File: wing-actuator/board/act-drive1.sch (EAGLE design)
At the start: 104 parts, among them J1 POWER_JACKPTH_LOCK, Q1 BSS123, Q2 BSS123, U5 Q50-5C, U7 LP2985-33, U8 TPS62160, X1 SMA-142-0701-801/806, X2 SMA-142-0701-801/806, X3 SMA-142-0701-801/806, X4 SMA-142-0701-801/806, X5 2516-

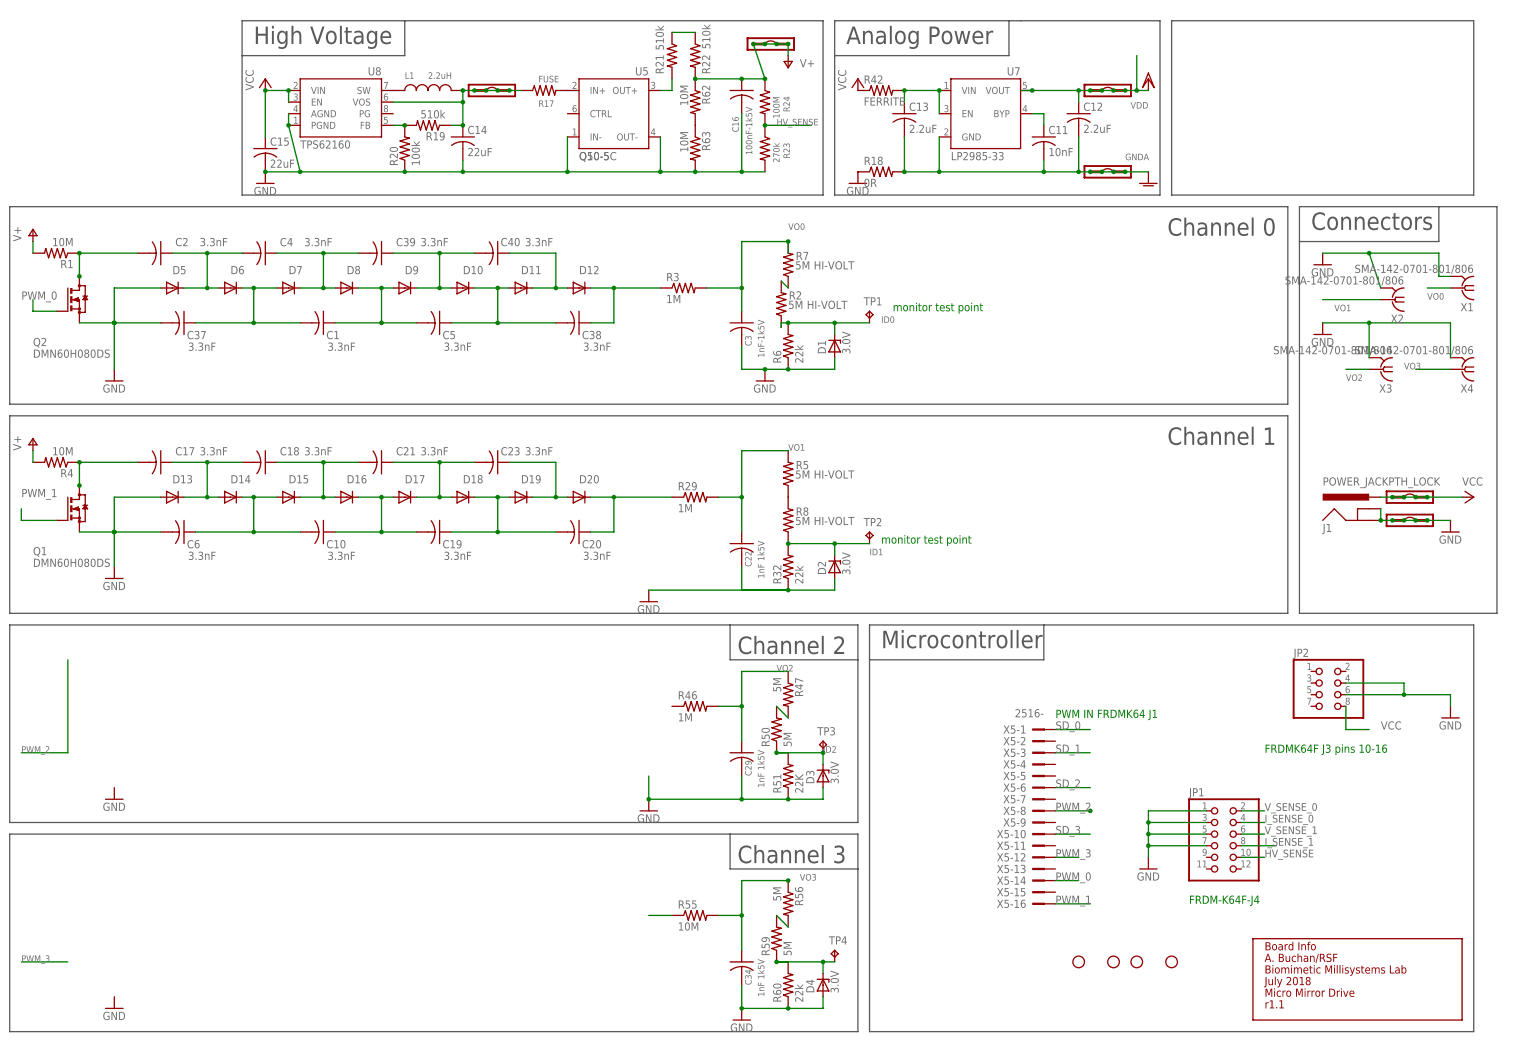
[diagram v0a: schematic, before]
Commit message: updated library to include 1:10 xfmr
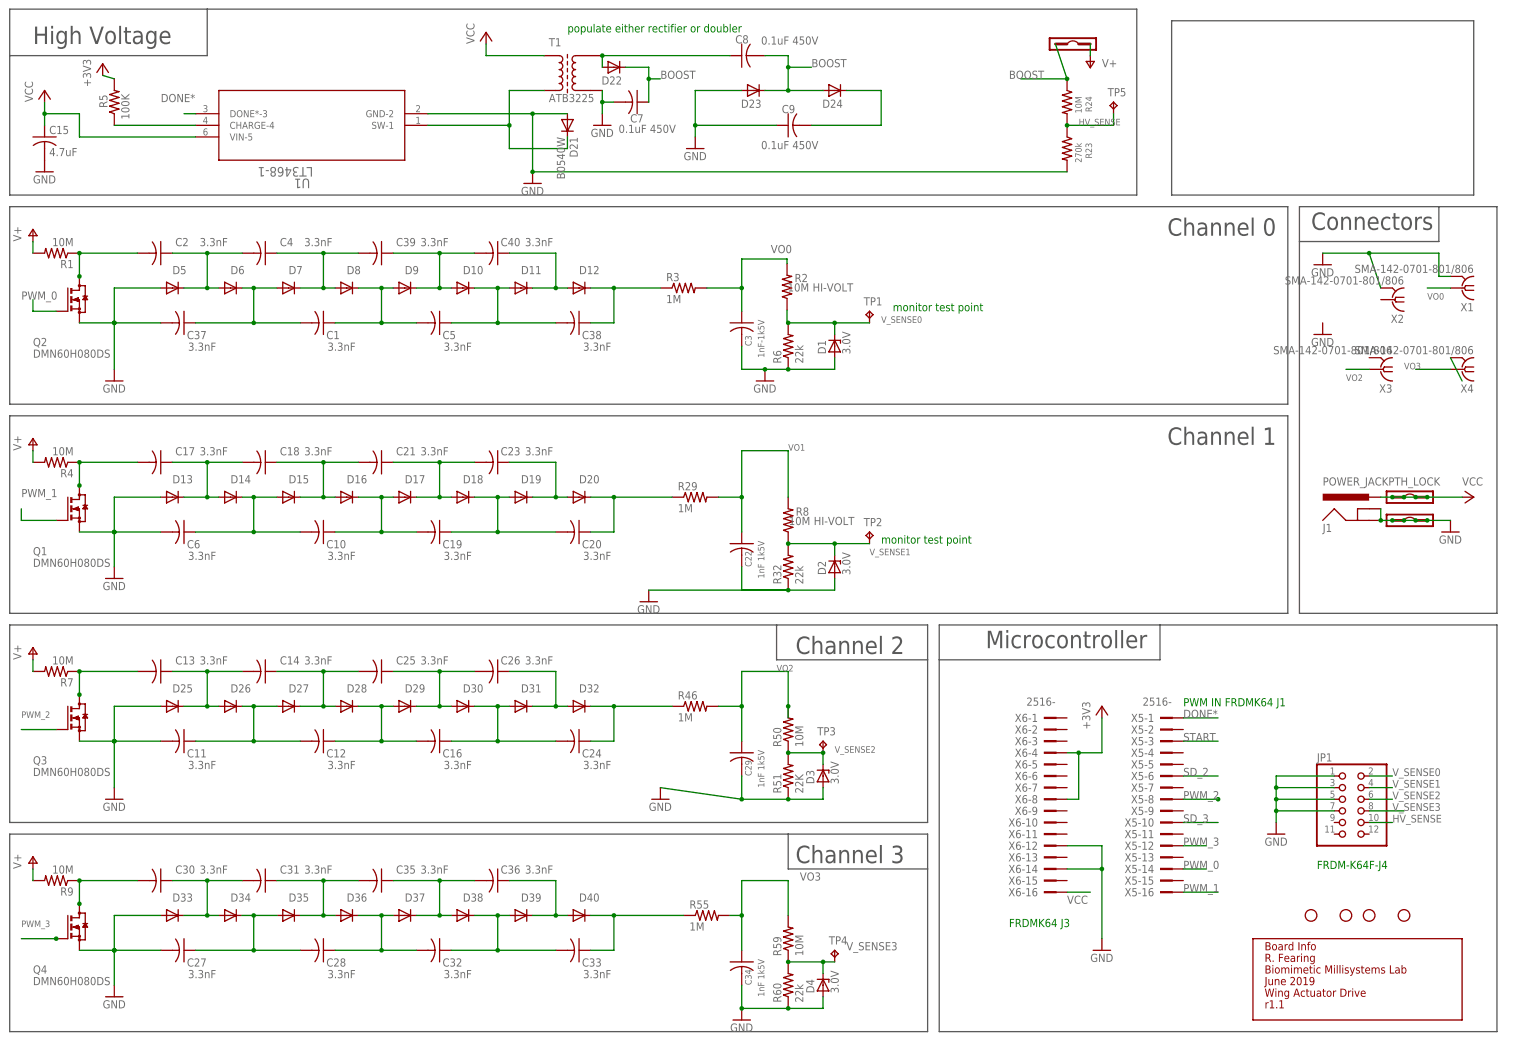
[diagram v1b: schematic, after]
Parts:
- removed GNDA, HV_IN, VDDA: (no value), modular_robotics:M04LOCK
- removed JP2: (no value), pinhead:PINHD-2X4
- removed L1: 2.2uH, modular_robotics:INDUCTOR
- removed R17: FUSE, rcl:R-US_R1206
- removed R18: 0R, rcl:R-US_R1206
- removed R19, R21, R22: 510k, rcl:R-US_R1206
- removed R20: 100k, rcl:R-US_R1206
- removed R42: FERRITE, rcl:R-US_R1206
- removed R47, R56: 5M, rcl:R-US_R1206
- removed R62, R63: 10M, rcl:R-US_R1206
- removed U5: Q50-5C, modular_robotics:Q50-5C
- removed U7: LP2985-33, modular_robotics:LP2985-33
- removed U8: TPS62160, modular_robotics:TPS62160
- added C24, C25, C26, C27, C28, C30, C31, C32, C33, C35, C36: 3.3nF, rcl:C-USC0805K
- added C7, C8, C9: 0.1uF 450V, rcl:C-USC1206
- added D21: B0540W, diode:DIODE-SOD123
- added D22, D23, D24, D25, D26, D27, D28, D29, D30, D31, D32, D33, D34, D35, D36, D37, D38, D39, D40: (no value), diode:DIODE-SOD323-W
- added Q3, Q4: BSS123, transistor-small-signal:BSS123
- added R9: 10M, rcl:R-US_R1206
- added T1: ATB3225, lt3468-1:ATB3225
- added TP5: TPTP10SQ, testpad:TPTP10SQ
- added U1: LT3468-1, ActuatorDrive:LT3468-1
- added X6: 2516-, con-3m:2516-
- C11: value 10nF -> 3.3nF; device rcl:C-USC1206 -> rcl:C-USC0805K
- C12, C13: value 2.2uF -> 3.3nF; device rcl:C-USC1206 -> rcl:C-USC0805K
- C14: value 22uF -> 3.3nF; device rcl:C-USC1206 -> rcl:C-USC0805K
- C15: value 22uF -> 4.7uF
- C16: value 100nF-1k5V -> 3.3nF; device rcl:C-USC2225K -> rcl:C-USC0805K
- R2, R50, R59: value 5M -> 10M; device rcl:R-US_R1206 -> rcl:R-US_R2010
- R24: value 100M -> 10M
- R5: value 5M -> 100K; device rcl:R-US_R1206 -> resistor:R-US_R1206; HI-VOLT 800 -> (none)
- R55: value 10M -> 1M
- R7: value 5M -> 10M; HI-VOLT 800 -> (none)
- R8: value 5M -> 10M; device rcl:R-US_R1206 -> rcl:R-US_R2010; HI-VOLT 800 -> 2000
- U$18: AUTHOR A. Buchan/RSF -> R. Fearing; DATE July 2018 -> June 2019; DESIGN Micro Mirror Drive -> Wing Actuator Drive
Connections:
- net SD_1 renamed START
- removed net GNDA: C11.2, C12.2, C13.2, GNDA.1, GNDA.2, GNDA.3, GNDA.4, R18.2, U7.GND
- removed net ID0: D1.C, R2.1, R6.2, TP1.TP
- removed net ID1: D2.C, R32.2, R8.1, TP2.TP
- removed net ID2: D3.C, R50.1, R51.2, TP3.TP
- removed net ID3: D4.C, R59.1, R60.2, TP4.TP
- removed net I_SENSE_0: JP1.4
- removed net I_SENSE_1: JP1.8
- removed net N$60: R21.2, U5.OUT+
- removed net N$62: R62.2, R63.1
- removed net SD_0: X5-1.KL
- removed net VDDA: C12.1, U7.VOUT, VDDA.1, VDDA.2, VDDA.3, VDDA.4
- removed net V_SENSE_0: JP1.2
- removed net V_SENSE_1: JP1.6
- new net +3V3: R5.2, X6-4.KL, X6-8.KL
- new net BOOST: C7.1, C8.2, D22.C, D23.C, D24.A, HV_OUT.4, R24.1
- new net DONE*: R5.1, U1.CHARGE-4, U1.DONE*-3, X5-1.KL
- new net N$28: X4.2
- new net N$29: C25.1, C26.2, D29.C, D30.A
- new net N$30: C13.2, Q3.D, R7.1
- new net N$32: C30.1, C31.2, D33.C, D34.A
- new net N$33: C27.1, C28.2, D34.C, D35.A
- new net N$34: C36.1, D39.C, D40.A
- new net N$35: C28.1, C32.2, D36.C, D37.A
- new net N$36: C32.1, C33.2, D38.C, D39.A
- new net N$38: C35.1, C36.2, D37.C, D38.A
- new net N$39: C30.2, Q4.D, R9.1
- new net V_SENSE0: D1.C, JP1.2, R2.1, R6.2, TP1.TP
- new net V_SENSE1: D2.C, JP1.4, R32.2, R8.1, TP2.TP
- new net V_SENSE2: D3.C, JP1.6, R50.1, R51.2, TP3.TP
- new net V_SENSE3: D4.C, JP1.8, R59.1, R60.2, TP4.TP
- net GND: now also C11.2, C27.2, C7.2, C9.1, D21.A, D23.A, D25.A, D33.A, Q3.S, Q4.S, T1.S3, X6-12.KL, X6-14.KL; no longer C14.2, C16.2, JP2.4, JP2.6, R18.1, R20.1, R63.2, U5.IN-, U5.OUT-, U8.AGND, U8.PGND, X3.2, X4.2
- net HV_SENSE: now also TP5.TP
- net N$12: now also D21.C, T1.P4; no longer R17.2, U5.IN+
- net N$17: now also C13.1, C14.2, D25.C, D26.A; no longer L1.1, U8.SW
- net N$18: now also C11.1, C12.2, D26.C, D27.A; no longer C14.1, HV_IN.1, HV_IN.2, HV_IN.3, HV_IN.4, L1.2, R17.1, R19.1, U8.VOS
- net N$19: now also C9.2, D24.C; no longer C11.1, U7.BYP
- net N$20: now also C26.1, D31.C, D32.A; no longer R19.2, R20.2, U8.FB
- net N$24: now also C12.1, C16.2, D28.C, D29.A; no longer R21.1, R22.1
- net N$25: now also C16.1, C24.2, D30.C, D31.A; no longer R47.2, R50.2
- net N$26: now also C33.1, D40.C
- net N$27: now also C14.1, C25.2, D27.C, D28.A; no longer R56.2, R59.2
- net N$37: now also C31.1, C35.2, D35.C, D36.A; no longer C13.1, R42.2, U7.EN, U7.VIN
- net N$4: now also C24.1, D32.C, R46.1; no longer R2.2, R7.1
- net N$6: now also C8.1, D22.A, T1.S2; no longer R5.1, R8.2
- net PWM_2: now also Q3.G
- net PWM_3: now also Q4.G
- net V+: now also R7.2, R9.2; no longer C16.1, HV_OUT.2, HV_OUT.3, HV_OUT.4, R22.2, R24.1, R62.1
- net VCC: now also T1.P1, U1.VIN-5, X6-16.KL; no longer JP2.8, R42.1, U8.EN, U8.VIN
- net VO0: now also R2.2; no longer R7.2
- net VO1: now also R8.2; no longer R5.2, X2.1
- net VO2: now also R50.2; no longer R47.1
- net VO3: now also R59.2; no longer R56.1
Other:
- note added: "FRDMK64 J3"
- note added: "populate either rectifier or doubler"
- note removed: "Analog Power"
- note removed: "FRDMK64F J3 pins 10-16"
- moved on the sheet: C11, C12, C13, C14, C15, C16, JP1, R2, R23, R24, R5, R50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

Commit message: placing flash boost converter
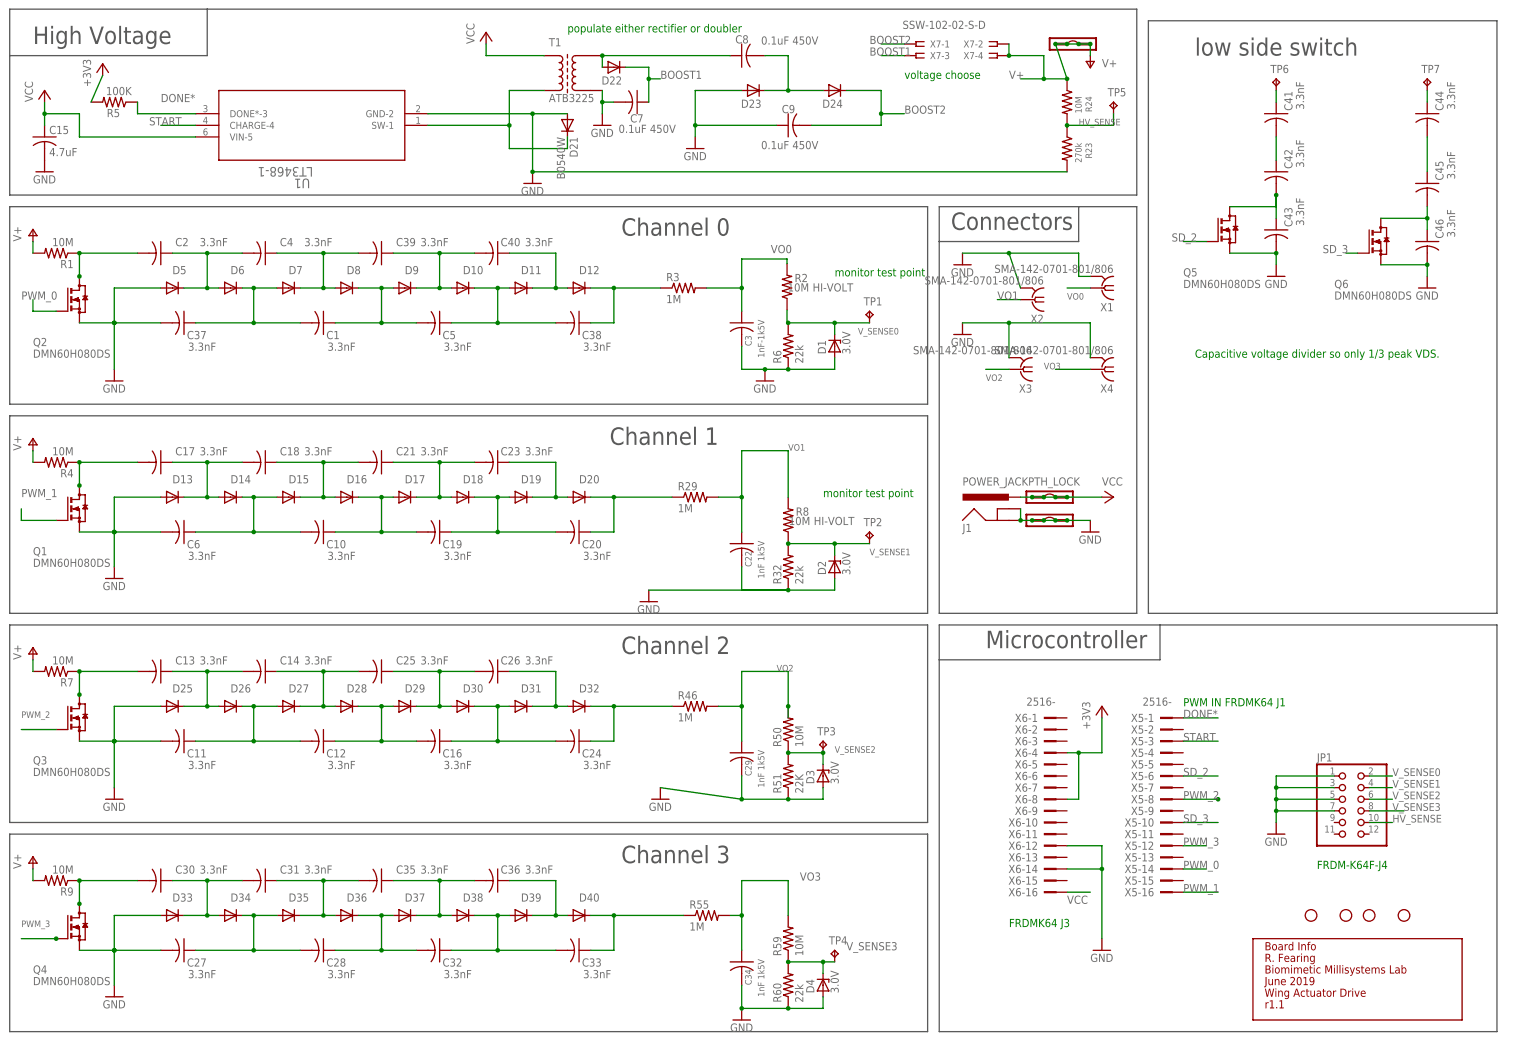
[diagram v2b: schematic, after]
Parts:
- added C41, C42, C43, C44, C45, C46: 3.3nF, rcl:C-USC0805K
- added Q5, Q6: BSS123, transistor-small-signal:BSS123
- added TP6, TP7: TPTP20SQ, testpad:TPTP20SQ
- added X7: SSW-102-02-S-D, con-samtec:SSW-102-02-S-D
- TP5: value TPTP10SQ -> TPTP20SQ; device testpad:TPTP10SQ -> testpad:TPTP20SQ
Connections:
- removed net N$19: C9.2, D24.C
- removed net N$28: X4.2
- new net BOOST1: C7.1, D22.C, X7-3.1
- new net BOOST2: C9.2, D24.C, X7-1.1
- new net N$40: C41.1, TP6.TP
- new net N$41: C41.2, C42.1
- new net N$42: C42.2, C43.1, Q5.D
- new net N$43: C44.1, TP7.TP
- new net N$44: C44.2, C45.1
- new net N$45: C45.2, C46.1, Q6.D
- net BOOST: no longer C7.1, D22.C, HV_OUT.4, R24.1
- net DONE*: no longer U1.CHARGE-4
- net GND: now also C43.2, C46.2, Q5.S, Q6.S, U1.GND-2, X3.2, X4.2
- net N$12: now also U1.SW-1
- net SD_2: now also Q5.G
- net SD_3: now also Q6.G
- net START: now also U1.CHARGE-4
- net V+: now also HV_OUT.2, HV_OUT.3, HV_OUT.4, R24.1, X7-2.1, X7-4.1
- net VO1: now also X2.1
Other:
- note added: "Capacitive voltage divider so only 1/3 peak VDS."
- note added: "low side switch"
- note added: "voltage choose"
- moved on the sheet: J1, R5, X1, X2, X3, X4

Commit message: started routing of wing actuator drive
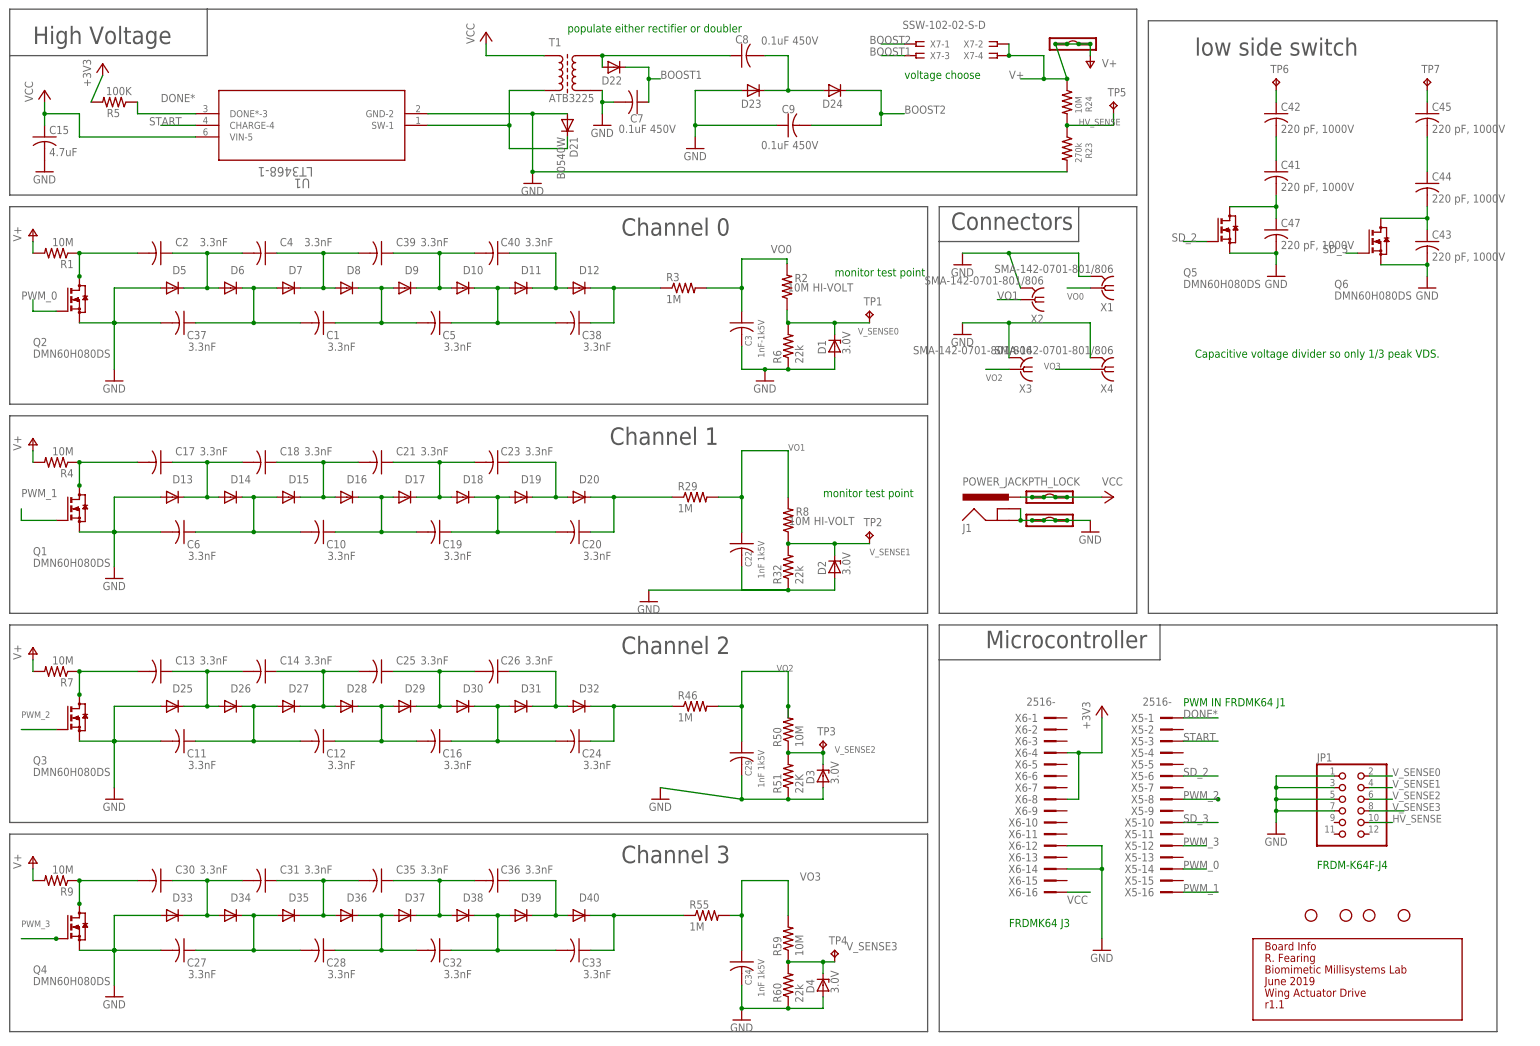
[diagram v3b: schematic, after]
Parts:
- removed C46: 3.3nF, rcl:C-USC0805K
- added C47: 220 pF, 1000V, rcl:C-USC1206
- C41, C42, C43, C44, C45: value 3.3nF -> 220 pF, 1000V; device rcl:C-USC0805K -> rcl:C-USC1206; DIGIKEY (none) -> 311-4469-1-ND
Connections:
- net GND: now also C47.2; no longer C46.2
- net N$40: now also C42.1; no longer C41.1
- net N$41: now also C41.1, C42.2; no longer C41.2, C42.1
- net N$42: now also C41.2, C47.1; no longer C42.2, C43.1
- net N$43: now also C45.1; no longer C44.1
- net N$44: now also C44.1, C45.2; no longer C44.2, C45.1
- net N$45: now also C43.1, C44.2; no longer C45.2, C46.1
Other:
- moved on the sheet: C41, C42, C43, C44, C45

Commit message: more routing and adding ground plane
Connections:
- net SD_2: now also X5-10.KL; no longer X5-6.KL
- net SD_3: now also X5-6.KL; no longer X5-10.KL
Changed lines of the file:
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@@
 <instance part="C47" gate="G$1" x="302.26" y="124.46" smashed="yes">
 <attribute name="NAME" x="303.276" y="125.095" size="1.778" layer="95"/>
-<attribute name="VALUE" x="303.276" y="120.269" size="1.778" layer="96"/>
+<attribute name="VALUE" x="303.276" y="127.889" size="1.778" layer="96"/>
 <attribute name="DIGIKEY" x="302.26" y="124.46" size="1.778" layer="96" display="off"/>
 </instance>
@@
 <net name="SD_2" class="0">
 <segment>
-<label x="281.94" y="5.08" size="1.778" layer="95"/>
-<pinref part="X5" gate="-6" pin="KL"/>
-<wire x1="289.56" y1="5.08" x2="281.94" y2="5.08" width="0.1524" layer="91"/>
+<label x="281.94" y="-5.08" size="1.778" layer="95"/>
+<pinref part="X5" gate="-10" pin="KL"/>
+<wire x1="289.56" y1="-5.08" x2="281.94" y2="-5.08" width="0.1524" layer="91"/>
 </segment>
 <segment>
@@
 <wire x1="287.02" y1="121.92" x2="281.94" y2="121.92" width="0.1524" layer="91"/>
 <label x="279.4" y="121.92" size="1.778" layer="95"/>
-</segment>
-</net>
-<net name="SD_3" class="0">
-<segment>
-<label x="281.94" y="-5.08" size="1.778" layer="95"/>
-<pinref part="X5" gate="-10" pin="KL"/>
-<wire x1="289.56" y1="-5.08" x2="281.94" y2="-5.08" width="0.1524" layer="91"/>
-</segment>
-<segment>
-<pinref part="Q6" gate="G$1" pin="G"/>
-<wire x1="320.04" y1="119.38" x2="317.5" y2="119.38" width="0.1524" layer="91"/>
-<label x="312.42" y="119.38" size="1.778" layer="95"/>
 </segment>
 </net>
@@
 </segment>
 </net>
+<net name="SD_3" class="0">
+<segment>
+<label x="281.94" y="5.08" size="1.778" layer="95"/>
+<pinref part="X5" gate="-6" pin="KL"/>
+<wire x1="289.56" y1="5.08" x2="281.94" y2="5.08" width="0.1524" layer="91"/>
+</segment>
+<segment>
+<pinref part="Q6" gate="G$1" pin="G"/>
+<wire x1="320.04" y1="119.38" x2="317.5" y2="119.38" width="0.1524" layer="91"/>
+<label x="312.42" y="119.38" size="1.778" layer="95"/>
+</segment>
+</net>
